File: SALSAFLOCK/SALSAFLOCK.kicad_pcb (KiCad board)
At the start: 2 copper layers, 6.3 x 6.4 mm, 7 parts, among them P1 INPUT, P2 ANTENNA, Q1 MOSFET_N

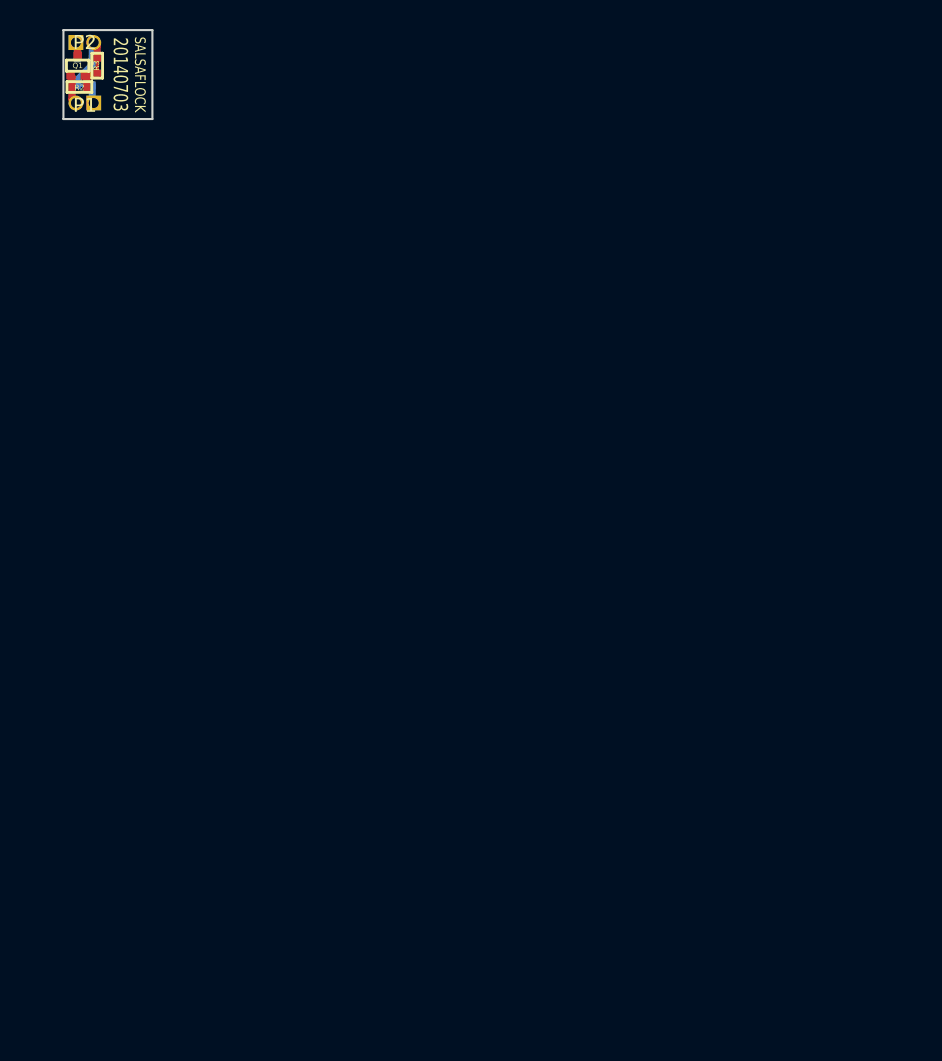
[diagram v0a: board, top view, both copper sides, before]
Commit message: connector layout
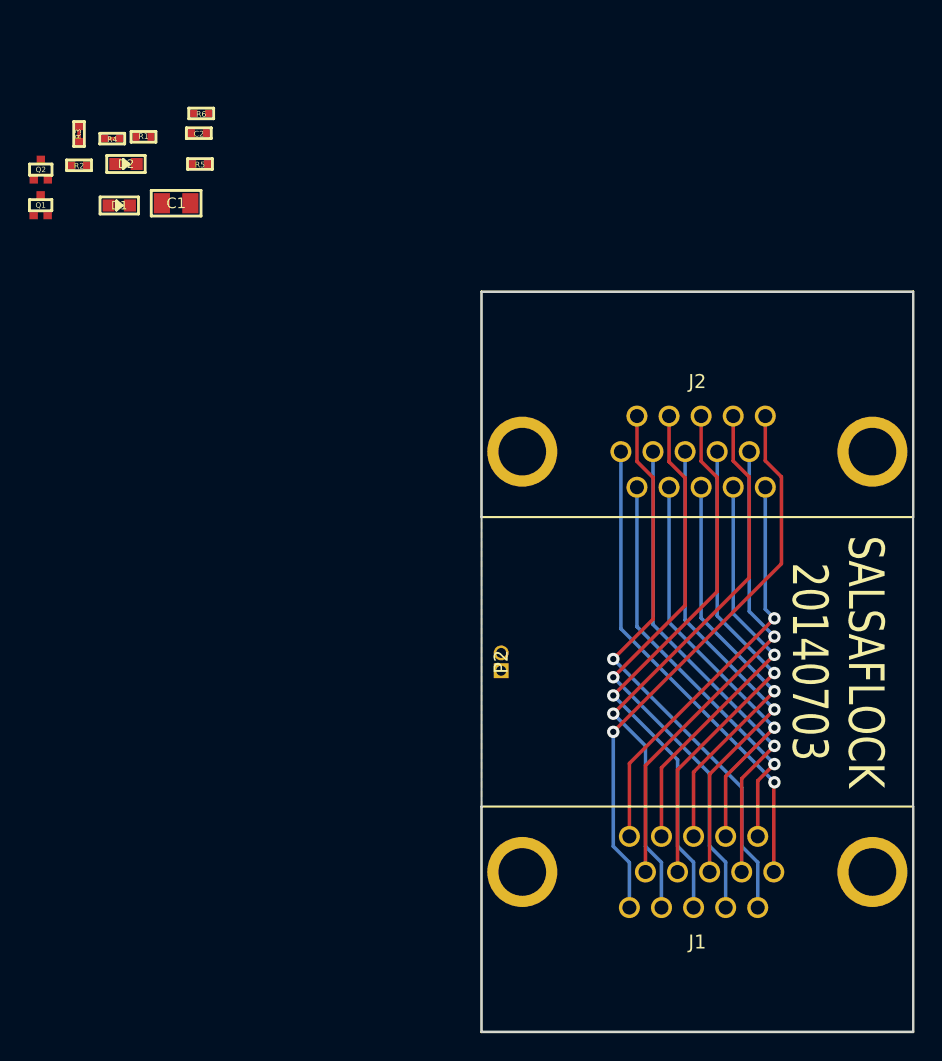
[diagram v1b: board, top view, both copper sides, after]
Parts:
- removed P1: INPUT, GSG-50MIL-HEADER-1x2-TH
- added C1: 22uF, GSG-0805, F.Cu at (87.8, 62.3)
- added C2: 1uF, GSG-0402, F.Cu at (89.4, 57.3)
- added D1: DIODE, GSG-0603D, F.Cu at (83.7, 62.4)
- added D2: DIODE, GSG-0603D, F.Cu at (84.2, 59.5)
- added J1: DB15-VGA, GSG-DB15-VGA, F.Cu at (125.0, 110.0)
- added J2: DB15-VGA, GSG-DB15-VGA, F.Cu at (125.0, 80.0)
- added Q2: MOSFET_N, GSG-SOT416-GDS, F.Cu at (78.1, 59.9)
- added R5: 10k, GSG-0402, F.Cu at (89.5, 59.5)
- added R6: 1M, GSG-0402, F.Cu at (89.6, 55.9)
- R1, R4: moved to F.Cu
- R2: value 100k -> 10k
- moved P2 53.3 mm to (111.0, 95.0), turned to 90 degrees
- moved Q1 10.3 mm to (78.1, 62.4)
- moved R1 6.98 mm to (85.5, 57.5)
- moved R2 5.59 mm to (80.9, 59.6)
- moved R3 5.05 mm to (80.9, 57.3)
- moved R4 4.29 mm to (83.2, 57.7)
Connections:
- R4 pad 2: N-000003 -> /VGAGND
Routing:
- net N-000005: track 0.00 -> 41.0 mm, vias 0 -> 1
- net N-000001: track 0.00 -> 41.0 mm, vias 0 -> 1
- net /SCL: track 0.00 -> 41.0 mm, vias 0 -> 1
- net N-000006: track 0.00 -> 41.0 mm, vias 0 -> 1
- net N-0000014: track 0.00 -> 41.0 mm, vias 0 -> 1
- net N-000004: track 0.00 -> 34.6 mm, vias 0 -> 1
- net /KEY: track 0.00 -> 34.6 mm, vias 0 -> 1
- net N-000002: track 0.00 -> 34.6 mm, vias 0 -> 1
- net N-0000016: track 0.00 -> 34.6 mm, vias 0 -> 1
- net N-000003: track 1.31 -> 34.6 mm, vias 0 -> 1
- net /RED: track 0.00 -> 29.5 mm, vias 0 -> 1
- net N-000007: track 0.00 -> 29.5 mm, vias 0 -> 1
- net N-0000011: track 0.00 -> 29.5 mm, vias 0 -> 1
- net N-0000010: track 0.00 -> 29.5 mm, vias 0 -> 1
- net /VGAGND: track 0.00 -> 29.5 mm, vias 0 -> 1
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- added copper zone on B.Cu, net /SHIELD
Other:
- board size 6.3 x 6.4 mm -> 30.8 x 52.8 mm
- net class Default: trace_width 0.508 -> 0.254
- rule via_min_drill: 0.508 -> 0.381
- rule via_min_size: 0.889 -> 0.6858
- board text removed: "0703"
- board text removed: "trim line"

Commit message: finished SALSAFLOCK
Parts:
- D1, D2: value DIODE -> DIODE-SOT23-3; footprint GSG-0603D -> GSG-SOT23-3
- Q1, Q2: footprint GSG-SOT416-GDS -> GSG-SOT143B-GDS
- moved R3 70.4 mm to (137.2, 99.6), turned to 180 degrees
- moved Q1 68.1 mm to (136.6, 97.4)
- moved R2 67.2 mm to (134.8, 99.6)
- moved Q2 66.7 mm to (133.3, 97.3), turned to 270 degrees
- moved R6 64.7 mm to (136.0, 100.9)
- moved R1 63.9 mm to (137.4, 94.8), turned to 90 degrees
- moved C2 62.2 mm to (133.7, 100.9)
- moved R4 60.0 mm to (132.5, 91.9), turned to 180 degrees
- moved D1 59.5 mm to (134.7, 93.2), turned to 180 degrees
- moved D2 57.0 mm to (133.2, 88.7), turned to 90 degrees
- moved C1 56.3 mm to (136.7, 90.2), turned to 270 degrees
- moved R5 53.7 mm to (135.4, 87.3), turned to 180 degrees
- moved P2 28.0 mm to (139.0, 95.0)
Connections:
- D1 pad 2: N-0000019 -> (no net)
- D2 pad 2: N-000008 (its old number) -> (no net)
- R5 pad 2: N-000008 (its old number) -> N-0000018
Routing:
- net N-0000019: track 0.00 -> 24.3 mm, vias 0 -> 2
- net /GATE: track 0.00 -> 7.18 mm
- net /KEY: track 34.6 -> 38.5 mm
- net /RED: track 29.5 -> 32.7 mm
- net /SOURCE: track 0.00 -> 3.05 mm
- net /DRAIN: track 0.00 -> 2.85 mm
- net N-0000018: track 0.00 -> 1.67 mm
- net GND: track 0.00 -> 1.64 mm
- net /VGAGND: track 29.5 -> 30.9 mm
- net /SCL: track 41.0 -> 42.3 mm
- added copper zone on F.Cu, net GND

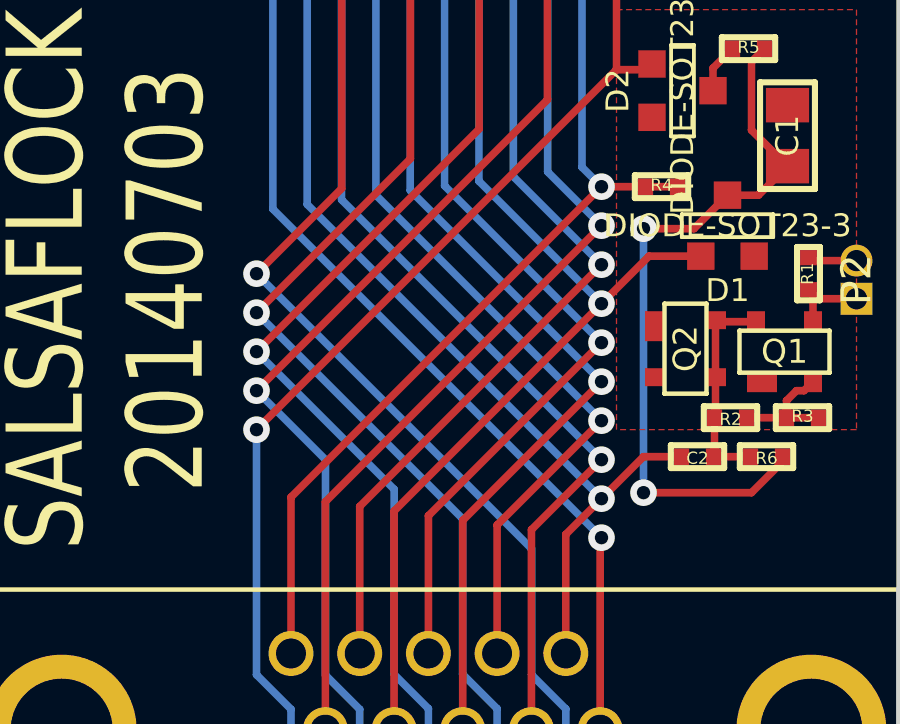
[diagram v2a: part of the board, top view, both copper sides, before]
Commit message: improved via annular ring
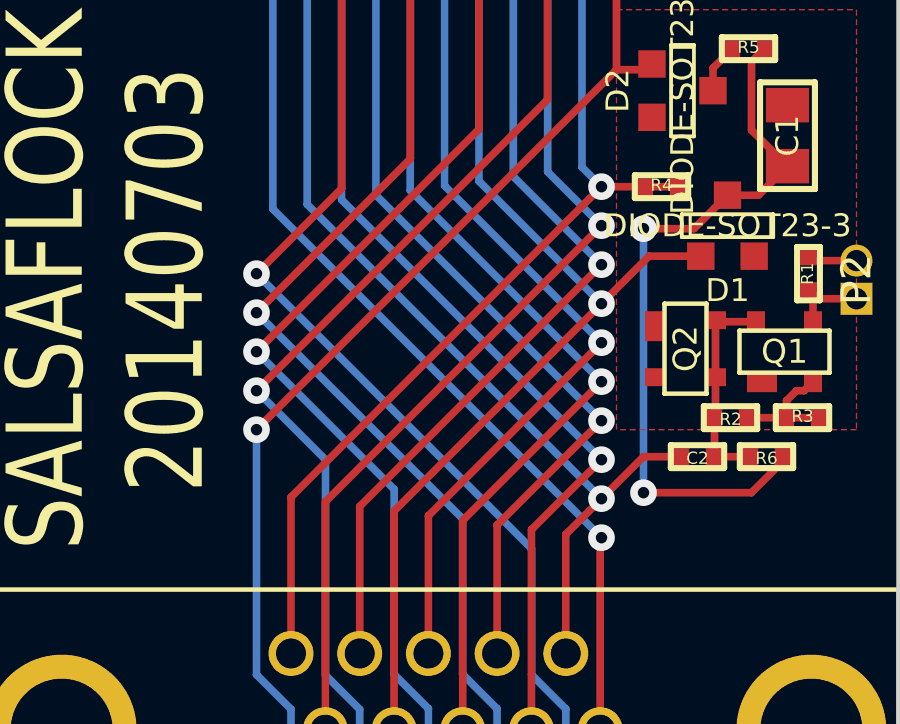
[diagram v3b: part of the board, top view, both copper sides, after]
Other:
- net class Default: via_drill 0.635 -> 0.381
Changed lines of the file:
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@@
     (links 40)
     (no_connects 2)
-    (area 76.134407 55.123399 146.492342 121.759001)
+    (area 102.507658 68.240999 140.739001 121.759001)
     (thickness 1.6)
     (drawings 6)
@@
     (edge_width 0.15)
     (via_size 0.889)
-    (via_drill 0.635)
+    (via_drill 0.381)
     (via_min_size 0.6858)
     (via_min_drill 0.381)
@@
     (visible_elements FFFFBFBF)
     (pcbplotparams
-      (layerselection 284196865)
+      (layerselection 283672577)
       (usegerberextensions true)
       (excludeedgelayer true)
@@
     (trace_width 0.254)
     (via_dia 0.889)
-    (via_drill 0.635)
+    (via_drill 0.381)
     (uvia_dia 0.508)
     (uvia_drill 0.127)

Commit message: updated date mark
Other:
- board text added: "20140728"
- board text removed: "20140703"
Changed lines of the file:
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@@
   (gr_line (start 109.6 121.4) (end 140.4 121.4) (angle 90) (layer Edge.Cuts) (width 0.15))
   (gr_line (start 109.6 68.6) (end 109.6 121.4) (angle 90) (layer Edge.Cuts) (width 0.15))
-  (gr_text 20140703 (at 116 95 90) (layer F.SilkS)
+  (gr_text 20140728 (at 116 95 90) (layer F.SilkS)
     (effects (font (size 2.54 2.032) (thickness 0.4064)))
   )
@@
   (segment (start 119 100) (end 131 88) (width 0.254) (layer F.Cu) (net 5))
   (via (at 119 100) (size 0.889) (layers F.Cu B.Cu) (net 5))
-  (segment (start 136.6666 99.6) (end 136.6666 99.0334) (width 0.254) (layer F.Cu) (net 7) (status 400000))
-  (segment (start 137.25 98.7) (end 137.55 98.4) (width 0.254) (layer F.Cu) (net 7) (status C00000))
-  (segment (start 137 98.7) (end 137.25 98.7) (width 0.254) (layer F.Cu) (net 7) (status 800000))
+  (segment (start 136.6666 99.6) (end 136.6666 99.0334) (width 0.254) (layer F.Cu) (net 7))
+  (segment (start 137.25 98.7) (end 137.55 98.4) (width 0.254) (layer F.Cu) (net 7))
+  (segment (start 137 98.7) (end 137.25 98.7) (width 0.254) (layer F.Cu) (net 7))
   (segment (start 136.6666 99.0334) (end 137 98.7) (width 0.254) (layer F.Cu) (net 7))
   (segment (start 135.3334 99.6) (end 136.6666 99.6) (width 0.254) (layer F.Cu) (net 7))
